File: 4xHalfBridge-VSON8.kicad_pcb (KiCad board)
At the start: 4 copper layers, 88.9 x 34.5 mm, 84 parts, among them U1 VSON8_Nexfet, U2 VSON8_Nexfet, U3 VSON8_Nexfet, U4 VSON8_Nexfet, U5 VSON8_Nexfet, U6 VSON8_Nexfet, U7 VSON8_Nexfet, U8 VSON8_Nexfet, U9 PowerStage_L

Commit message: continue routing
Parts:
- removed the C14 at (214.9, 84.7)
- removed the C30 at (232.3, 93.7)
- removed the C32 at (199.4, 67.2)
- removed C35: C, Capacitor_SMD:C_1206_3216Metric_Pad1.42x1.75mm_HandSolder
- removed C36: C, Capacitor_SMD:C_0805_2012Metric_Pad1.15x1.40mm_HandSolder
- removed FB1, FB3, FB4, FB5, FB7, FB8: Ferrite_Bead, Inductor_SMD:L_0603_1608Metric_Pad1.05x0.95mm_HandSolder
- removed the R10 at (256.1, 38.6)
- removed the R21 at (220.0, 85.3)
- removed the R24 at (173.1, 51.4)
- removed the R27 at (241.8, 85.4)
- removed the R9 at (173.3, 46.4)
- removed the U8 at (245.8, 80.2)
- added C19: C, Capacitor_SMD:C_0603_1608Metric_Pad1.05x0.95mm_HandSolder, F.Cu at (47.9, 21.6)
- added C23: CP, Capacitor_THT:CP_Radial_D10.0mm_P5.00mm, F.Cu at (68.0, 32.5)
- added C27: CP, Capacitor_THT:CP_Radial_D5.0mm_P2.50mm, F.Cu at (35.9, 4.50)
- added R16: R, Resistor_SMD:R_0603_1608Metric_Pad1.05x0.95mm_HandSolder, F.Cu at (61.7, 21.2)
- added R2: R, Resistor_SMD:R_0603_1608Metric_Pad1.05x0.95mm_HandSolder, F.Cu at (26.5, 21.3)
- added R22: R, Resistor_SMD:R_1806_4516Metric_Pad1.57x1.80mm_HandSolder, F.Cu at (55.8, 22.4)
- added R23: R, Resistor_SMD:R_0603_1608Metric_Pad1.05x0.95mm_HandSolder, F.Cu at (45.7, 31.0)
- added R6: R, Resistor_SMD:R_0603_1608Metric_Pad1.05x0.95mm_HandSolder, F.Cu at (14.9, 27.5)
- added U3: PowerStage_L, sDrive_Carriers:PowerStage_Carrier_L, F.Cu at (0.00, 0.00)
- R11: renamed from R3; moved to B.Cu
- R12: renamed from R14; moved to B.Cu
- R18: renamed from R4; moved to B.Cu
- R19: renamed from R13; moved to B.Cu
- R27: renamed from R7; moved to B.Cu
- R28: renamed from R16; moved to B.Cu
- R30: footprint Resistor_SMD:R_0603_1608Metric_Pad1.05x0.95mm_HandSolder -> Resistor_SMD:R_1806_4516Metric_Pad1.57x1.80mm_HandSolder
- R4: renamed from R8; moved to B.Cu
- R5: renamed from R12; moved to B.Cu
- U9: value PowerStage_L -> VSON8_Nexfet; footprint sDrive_Carriers:PowerStage_Carrier_L -> Custom_Mosfet:MOSFET_CSD19531Q5A
- moved D1 230.9 mm to (44.1, 27.6), turned to 270 degrees
- moved C4 226.1 mm to (13.4, 27.5), turned to 270 degrees
- moved R21 205.6 mm to (44.1, 31.0), turned to 270 degrees
- moved R3 199.6 mm to (13.5, 18.2), turned to 90 degrees
- moved R20 196.8 mm to (56.0, 27.5), turned to 270 degrees
- moved C15 196.1 mm to (63.4, 8.10), turned to 270 degrees
- moved C7 191.2 mm to (16.6, 21.6), turned to 90 degrees
- moved C16 190.5 mm to (63.2, 21.2), turned to 270 degrees
- moved C3 190.3 mm to (15.1, 18.2), turned to 90 degrees
- moved C31 188.7 mm to (70.9, 4.40), turned to 180 degrees
- moved C25 188.5 mm to (81.0, 8.10), turned to 270 degrees
- moved F1 188.3 mm to (29.8, 29.8)
- moved R15 187.4 mm to (61.9, 8.10), turned to 270 degrees
- moved C6 186.1 mm to (15.1, 21.6), turned to 90 degrees
- moved C22 184.3 mm to (21.9, 32.5)
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- renumbered C4 to C1, C17 to C10, C27 to C11, C18 to C12, C19 to C13, C20 to C14, C2 to C15, C6 to C16, C13 to C17, C26 to C18, C5 to C2, C15 to C20, C16 to C21, C29 to C22, C31 to C24, C3 to C25, C8 to C26, C21 to C28, C33 to C29, C9 to C3, C28 to C30, C34 to C31, C22 to C32, C23 to C33, C24 to C34, C25 to C4, C10 to C5, C11 to C6, C12 to C7, C1 to C8, C7 to C9, R6 to R1, R19 to R10, R26 to R13, R22 to R14, R2 to R15, R18 to R17, R25 to R20, R29 to R21, R5 to R24, R15 to R25, R23 to R26, R28 to R29, R17 to R3, R20 to R7, R1 to R8, R11 to R9, U4 to U1, U5 to U2, U1 to U4, U7 to U5, U2 to U6, U6 to U7, U3 to U8
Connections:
- net Net-(C13-Pad2) renamed /CISENP
- net Net-(C17-Pad2) renamed /BISENP
- net Net-(C9-Pad2) renamed /AISENP
- C10 pad 1: Net-(C17-Pad1) (its old number) -> Net-(C10-Pad1)
- C11 pad 1: Net-(C18-Pad1) -> GND
- C12 pad 1: Net-(C18-Pad1) -> GND
- C12 pad 2: Net-(C17-Pad1) (its old number) -> Net-(C10-Pad1)
- C13 pad 1: Net-(C18-Pad1) -> GND
- C13 pad 2: Net-(C17-Pad1) (its old number) -> Net-(C10-Pad1)
- C14 pad 1: Net-(C18-Pad1) -> GND
- C14 pad 2: Net-(C17-Pad1) (its old number) -> Net-(C10-Pad1)
- C26 pad 1: Net-(C8-Pad1) (its old number) -> Net-(C26-Pad1)
- C28 pad 1: Net-(C21-Pad1) -> Net-(C28-Pad1)
- C32 pad 2: Net-(C21-Pad1) -> Net-(C28-Pad1)
- C33 pad 2: Net-(C21-Pad1) -> Net-(C28-Pad1)
- C34 pad 2: Net-(C21-Pad1) -> Net-(C28-Pad1)
- C4 pad 1: Net-(C10-Pad1) -> GND
- C4 pad 2: Net-(C25-Pad2) -> /AISENN
- C5 pad 1: Net-(C10-Pad1) -> GND
- C6 pad 1: Net-(C10-Pad1) -> GND
- C7 pad 1: Net-(C10-Pad1) -> GND
- D2 pad 1: Net-(D2-Pad1) -> GND
- R10 pad 1: Net-(C17-Pad1) (its old number) -> Net-(C10-Pad1)
- R13 pad 1: Net-(C18-Pad1) -> GND
- R14 pad 1: Net-(C17-Pad1) (its old number) -> Net-(C10-Pad1)
- R14 pad 2: Net-(C18-Pad1) -> GND
- R25 pad 1: Net-(C8-Pad1) (its old number) -> Net-(C26-Pad1)
- R26 pad 1: Net-(C21-Pad1) -> Net-(C28-Pad1)
- R28 pad 1: Net-(C8-Pad1) (its old number) -> Net-(C26-Pad1)
- R30 pad 1: Net-(D2-Pad2) -> Net-(C28-Pad1)
- R30 pad 2: /VDRAIN -> GND
- R7 pad 2: Net-(C10-Pad1) -> GND
- U5 pad 1: Net-(U7-Pad1) -> Net-(C10-Pad1)
- U9 pad 1: Net-(U9-Pad1) -> Net-(C28-Pad1)
- U9 pad 2: Net-(U9-Pad2) -> Net-(C26-Pad1)
- U9 pad 3: Net-(U9-Pad3) -> /D
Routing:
- net /VDRAIN: track 0.00 -> 121.1 mm
- net /BHG: track 16.0 -> 1.51 mm
- net VCC: track 0.00 -> 11.9 mm
- net /B: track 0.00 -> 5.16 mm
- net /BLG: track 5.66 -> 1.52 mm
- net Net-(C25-Pad1): track 0.00 -> 3.73 mm
- net Net-(C15-Pad1): track 0.00 -> 3.67 mm
- net Net-(C26-Pad1): track 0.00 -> 3.66 mm
- net Net-(C9-Pad1): track 0.00 -> 3.66 mm
- net Net-(C8-Pad1): track 0.00 -> 3.57 mm
- net Net-(C1-Pad1): track 0.00 -> 3.49 mm
- net Net-(C16-Pad1): track 0.00 -> 3.48 mm
- net Net-(C2-Pad1): track 0.00 -> 3.29 mm
- net /BISENN: track 3.53 -> 1.52 mm, vias 1 -> 0
- net Net-(D1-Pad2): track 0.00 -> 1.66 mm
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- added copper zone on F.Cu, net /A
- added copper zone on F.Cu, net /D
- added copper zone on B.Cu, net GND
- added copper zone on F.Cu, net Net-(C1-Pad1)
- added copper zone on F.Cu, net Net-(C10-Pad1)
- added copper zone on F.Cu, net Net-(C28-Pad1)
- added copper zone on F.Cu, net Net-(C3-Pad1)
- added copper zone on F.Cu, net VCC
- removed copper zone on F.Cu, net /BHG
- removed copper zone on F.Cu, net Net-(C15-Pad1)
- removed copper zone on F.Cu, net Net-(C16-Pad1)
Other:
- board size 88.9 x 34.5 mm -> 90 x 36 mm
- rule trace_min: 0.2 -> 0.2286

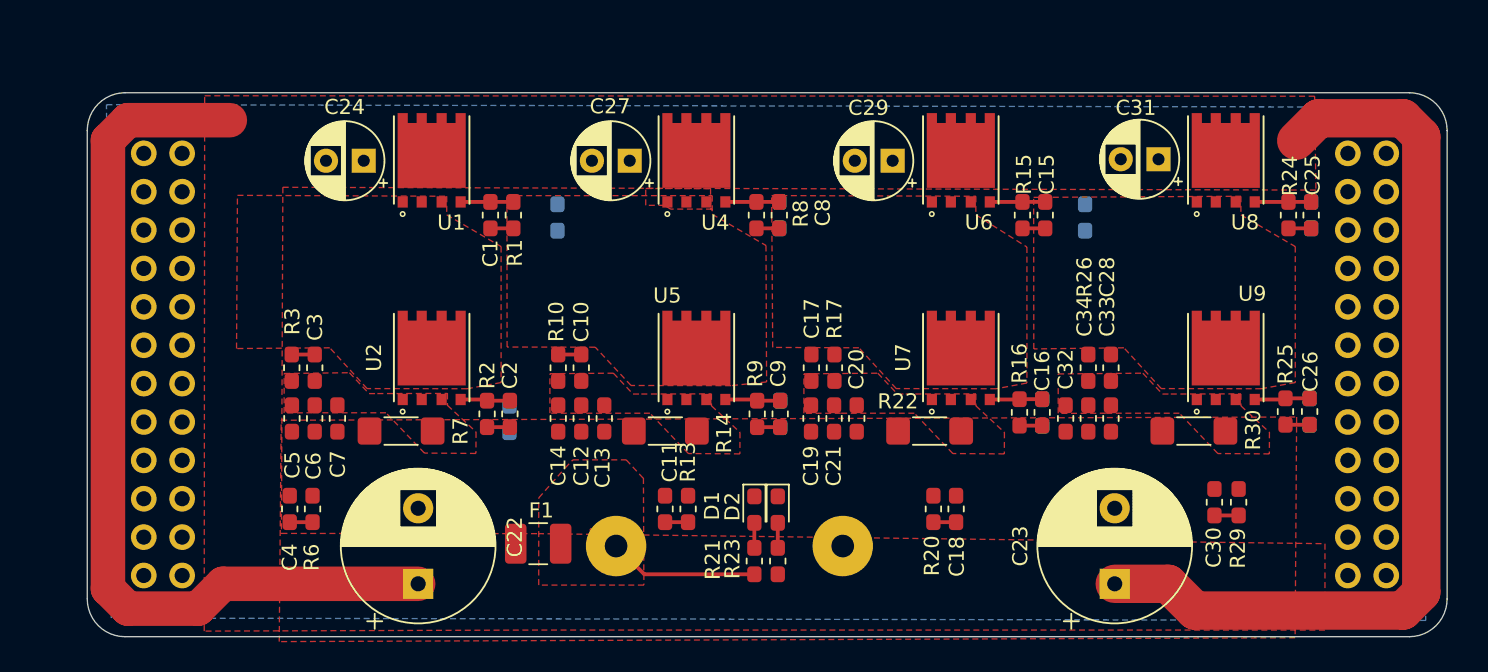
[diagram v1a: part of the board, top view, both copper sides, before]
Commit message: finalize pcb without eeprom
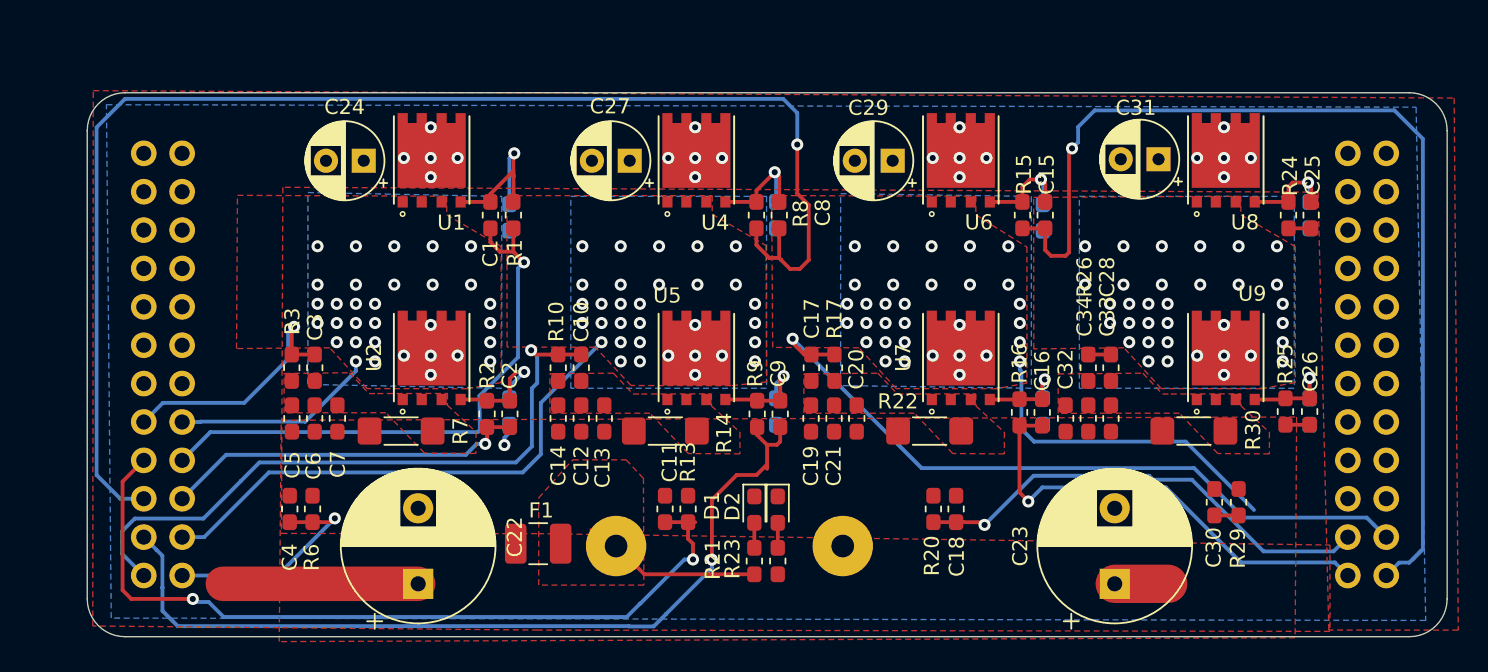
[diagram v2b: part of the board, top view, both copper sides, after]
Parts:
- moved R4 3.17 mm to (27.9, 8.26)
- moved R18 2.79 mm to (63.2, 8.26)
- moved R5 0.49 mm to (27.9, 21.1)
- moved R12 0.31 mm to (45.6, 21.1)
- moved R11 0.21 mm to (45.6, 8.10)
- moved R27 0.10 mm to (80.9, 8.10)
- moved R19 0.07 mm to (63.2, 21.1)
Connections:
- C1 pad 2: Net-(C1-Pad2) -> /AHG
- R1 pad 2: Net-(C1-Pad2) -> /AHG
- U3 pad 15: Net-(U3-Pad15) -> /AISENP
- U3 pad 16: Net-(U3-Pad16) -> /A
- U3 pad 17: Net-(U3-Pad17) -> /BISENN
- U3 pad 18: Net-(U3-Pad18) -> /AHG
- U3 pad 19: Net-(U3-Pad19) -> /BHG
- U3 pad 20: Net-(U3-Pad20) -> /ALG
- U3 pad 21: Net-(U3-Pad21) -> /BLG
- U3 pad 22: Net-(U3-Pad22) -> /B
- U3 pad 23: Net-(U3-Pad23) -> /BISENP
- U3 pad 24: Net-(U3-Pad24) -> /AISENN
- U3 pad 45: Net-(U3-Pad45) -> /CISENN
- U3 pad 46: Net-(U3-Pad46) -> /CISENP
- U3 pad 47: Net-(U3-Pad47) -> /CLG
- U3 pad 48: Net-(U3-Pad48) -> /CHG
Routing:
- net /VDRAIN: track 121.1 -> 16.5 mm, vias 0 -> 20
- net /BHG: track 1.51 -> 91.8 mm, vias 0 -> 1
- net /CHG: track 1.51 -> 68.5 mm, vias 0 -> 1
- net /BLG: track 1.52 -> 57.9 mm, vias 0 -> 1
- net /BISENN: track 1.52 -> 53.8 mm, vias 0 -> 2
- net /CISENP: track 0.00 -> 48.1 mm, vias 0 -> 1
- net /BISENP: track 1.52 -> 43.1 mm, vias 0 -> 1
- net /AHG: track 0.00 -> 38.6 mm, vias 0 -> 1
- net /B: track 5.16 -> 40.3 mm, vias 0 -> 32
- net /CISENN: track 1.50 -> 31.3 mm, vias 0 -> 1
- net /CLG: track 1.50 -> 30.7 mm, vias 0 -> 1
- net /ALG: track 1.51 -> 24.2 mm, vias 0 -> 1
- net /C: track 0.00 -> 22.1 mm, vias 0 -> 32
- net /AISENP: track 1.52 -> 17.0 mm, vias 0 -> 1
- net /A: track 0.00 -> 13.5 mm, vias 0 -> 32
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- added copper zone on B.Cu, net /A
- added copper zone on B.Cu, net /B
- added copper zone on B.Cu, net /C
- added copper zone on B.Cu, net /D
- removed copper zone on F.Cu, net Net-(C1-Pad1)
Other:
- net class Default: clearance 0.2 -> 0.254
- rule trace_clearance: 0.2 -> 0.254

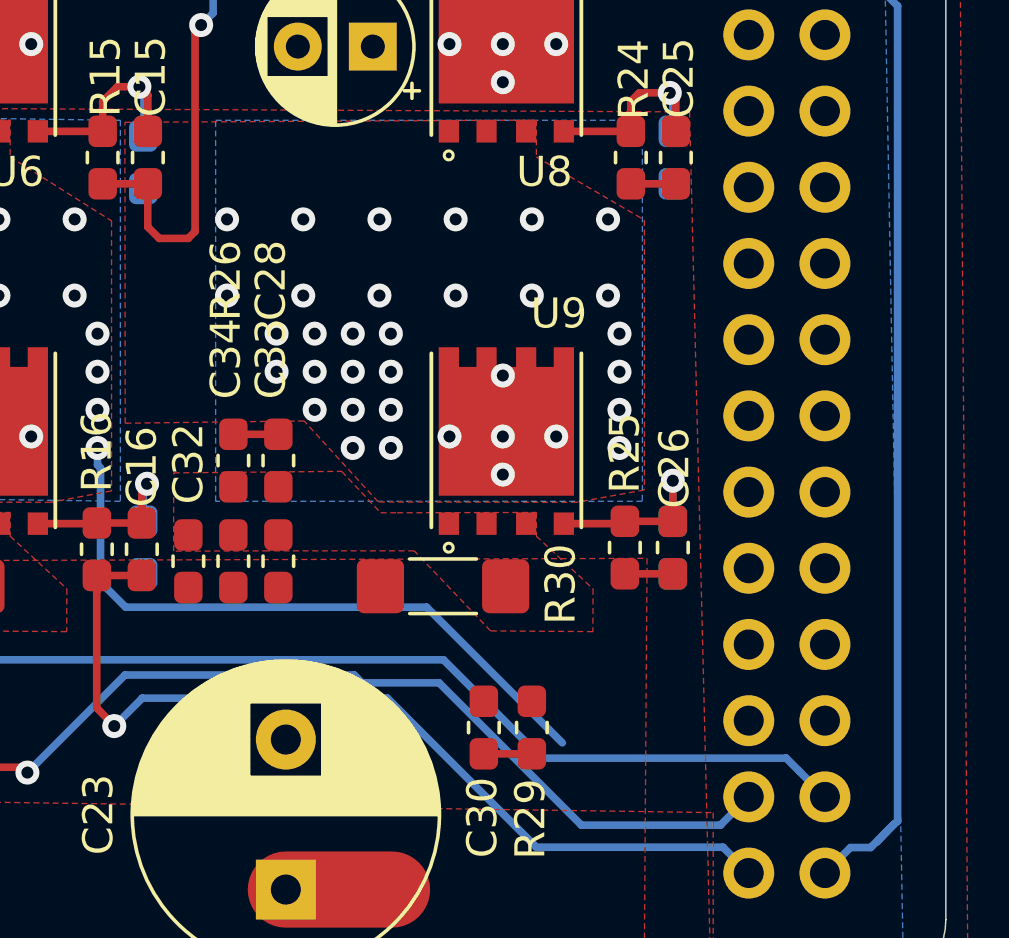
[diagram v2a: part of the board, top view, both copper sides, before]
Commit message: Update 4xHalfBridge-VSON8.kicad_pcb
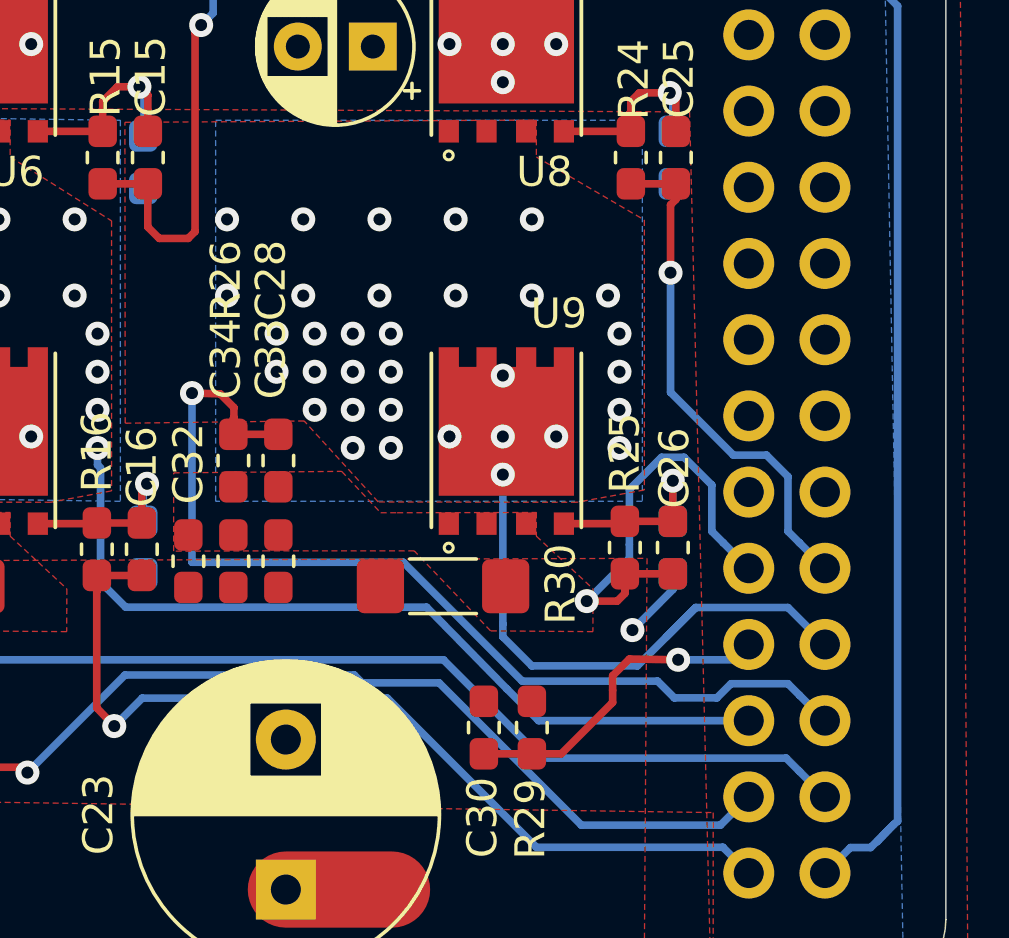
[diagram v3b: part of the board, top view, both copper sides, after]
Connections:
- U3 pad 39: Net-(U3-Pad39) -> /DLG
- U3 pad 40: Net-(U3-Pad40) -> /DHG
- U3 pad 41: Net-(U3-Pad41) -> /DISENN
- U3 pad 42: Net-(U3-Pad42) -> /D
- U3 pad 43: Net-(U3-Pad43) -> /C
- U3 pad 44: Net-(U3-Pad44) -> /DISENP
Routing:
- net /DISENP: track 1.50 -> 33.3 mm, vias 0 -> 1
- net /D: track 0.00 -> 19.2 mm, vias 34 -> 33
- net /DHG: track 1.50 -> 17.2 mm, vias 0 -> 1
- net /DLG: track 1.60 -> 14.8 mm, vias 0 -> 1
- net /DISENN: track 1.60 -> 10.9 mm, vias 0 -> 1
- net /C: track 22.1 -> 28.0 mm
- net GND: track 1.50 -> 3.94 mm, vias 1 -> 2

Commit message: finalize schematic and PCB
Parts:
- added C35: X7R, 47-nF, Capacitor_SMD:C_0603_1608Metric_Pad1.05x0.95mm_HandSolder, B.Cu at (11.3, 5.14)
- added D3: LED, LED_SMD:LED_0603_1608Metric_Pad1.05x0.95mm_HandSolder, B.Cu at (10.2, 19.1)
- added D4: D_Schottky, Diode_SMD:D_0603_1608Metric_Pad1.05x0.95mm_HandSolder, B.Cu at (9.85, 14.6)
- added F2: Fuse, Fuse:Fuse_0603_1608Metric_Pad1.05x0.95mm_HandSolder, B.Cu at (9.83, 16.1)
- added R31: R, Resistor_SMD:R_0603_1608Metric_Pad1.05x0.95mm_HandSolder, B.Cu at (9.84, 17.6)
- added R32: R, Resistor_SMD:R_0603_1608Metric_Pad1.05x0.95mm_HandSolder, B.Cu at (12.8, 5.14)
- added R33: R, Resistor_SMD:R_0603_1608Metric_Pad1.05x0.95mm_HandSolder, B.Cu at (10.6, 12.1)
- added R34: R, Resistor_SMD:R_0603_1608Metric_Pad1.05x0.95mm_HandSolder, B.Cu at (9.06, 12.1)
- added R35: R, Resistor_SMD:R_0603_1608Metric_Pad1.05x0.95mm_HandSolder, B.Cu at (9.22, 6.05)
- added R36: R, Resistor_SMD:R_0603_1608Metric_Pad1.05x0.95mm_HandSolder, B.Cu at (13.1, 12.2)
- added U10: 24LC01, Package_DFN_QFN:DFN-8-1EP_3x2mm_P0.5mm_EP1.75x1.45mm, B.Cu at (12.5, 8.61)
- renumbered C8 to C1, C5 to C10, C6 to C11, C7 to C12, C17 to C13, C19 to C14, C20 to C15, C21 to C16, C10 to C17, C12 to C18, C13 to C19, C15 to C2, C14 to C20, C28 to C21, C32 to C22, C33 to C23, C34 to C24, C4 to C25, C18 to C26, C11 to C27, C30 to C28, C22 to C29, C25 to C3, C23 to C30, C24 to C31, C27 to C32, C29 to C33, C31 to C34, C1 to C4, C2 to C5, C16 to C6, C9 to C7, C26 to C8, C3 to C9, R8 to R1, R16 to R10, R9 to R11, R5 to R12, R19 to R13, R12 to R14, R25 to R15, R28 to R16, R3 to R17, R17 to R18, R10 to R19, R15 to R2, R7 to R20, R22 to R21, R14 to R22, R26 to R23, R6 to R24, R20 to R25, R13 to R26, R30 to R27, R29 to R28, R21 to R29, R11 to R3, R23 to R30, R18 to R4, R24 to R5, R1 to R6, R27 to R7, R4 to R8, R2 to R9, U4 to U1, U6 to U2, U8 to U3, U1 to U4, U2 to U5, U7 to U6, U5 to U7, U9 to U8, U3 to U9
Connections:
- U9 pad 10: Net-(U3-Pad10) -> /SCL
- U9 pad 11: Net-(U3-Pad11) -> /5V
- U9 pad 12: Net-(U3-Pad12) -> /SDA
- U9 pad 9: Net-(U3-Pad9) -> /WP
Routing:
- net GND: track 3.94 -> 21.0 mm, vias 2 -> 5
- net /5V: track 0.00 -> 15.7 mm
- net /WP: track 0.00 -> 14.7 mm
- net Net-(C35-Pad1): track 0.00 -> 13.4 mm, vias 0 -> 2
- net /VDRAIN: track 16.5 -> 3.54 mm
- net /SDA: track 0.00 -> 11.5 mm, vias 0 -> 2
- net /SCL: track 0.00 -> 10.1 mm
- net Net-(R32-Pad2): track 0.00 -> 8.97 mm
- net Net-(R36-Pad1): track 0.00 -> 7.72 mm
- net Net-(D4-Pad2): track 0.00 -> 3.00 mm
- net Net-(R35-Pad2): track 0.00 -> 2.98 mm
- net /AISENP: track 17.0 -> 19.2 mm
- net Net-(D3-Pad2): track 0.00 -> 1.72 mm
- net /D: vias 33 -> 29
- net /C: vias 32 -> 28
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- added copper zone on B.Cu, net Net-(C35-Pad1)
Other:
- net class Default: clearance 0.254 -> 0.1524
- rule trace_clearance: 0.254 -> 0.1524
- rule trace_min: 0.2286 -> 0.2032
- board text added: "GND"
- board text added: "Vmot"
